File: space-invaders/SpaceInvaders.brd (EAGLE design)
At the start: 101.6 x 95.2 mm, 26 parts, among them J2-J4 TM4C123GXL, J3-J1 TM4C123GXL, J5 Nokia_5110, J6 Nokia_5110, J7 9V, U1 LM7805CT

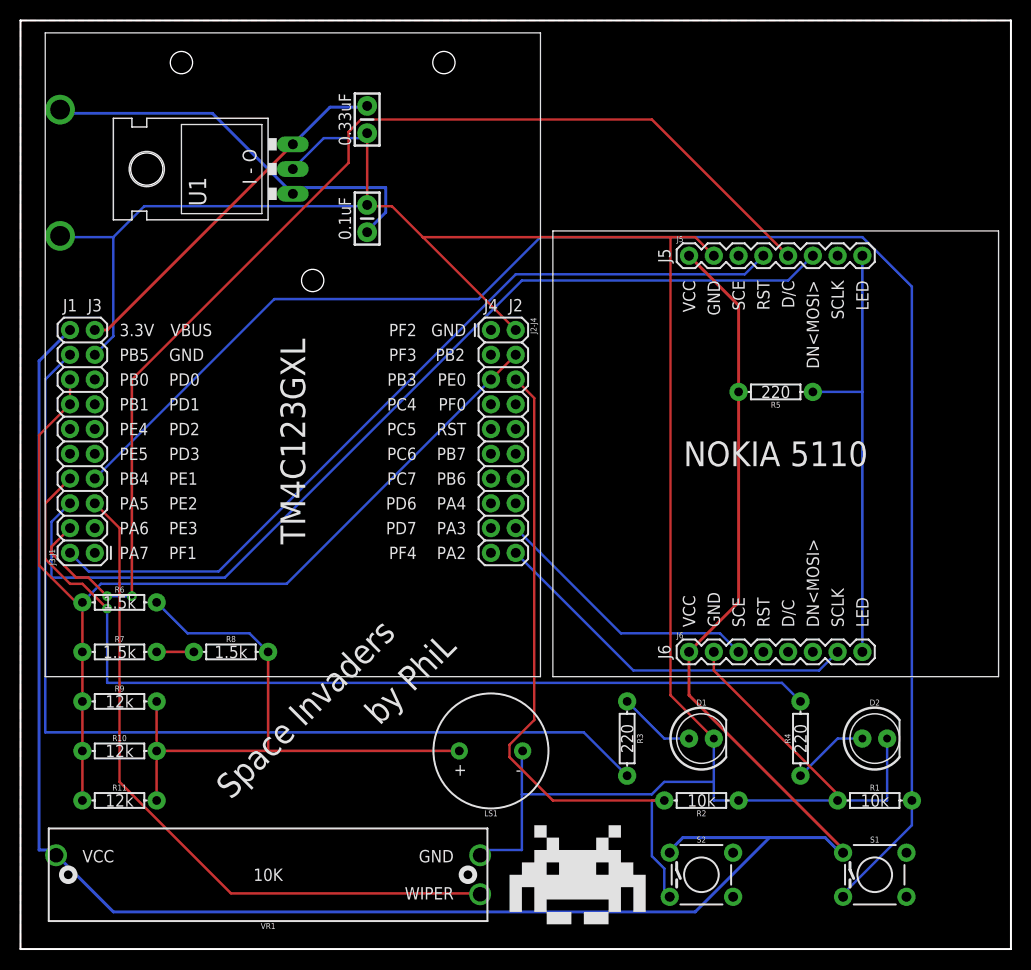
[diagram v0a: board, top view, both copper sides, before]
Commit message: Rip off Autorouter. Will route by hand.
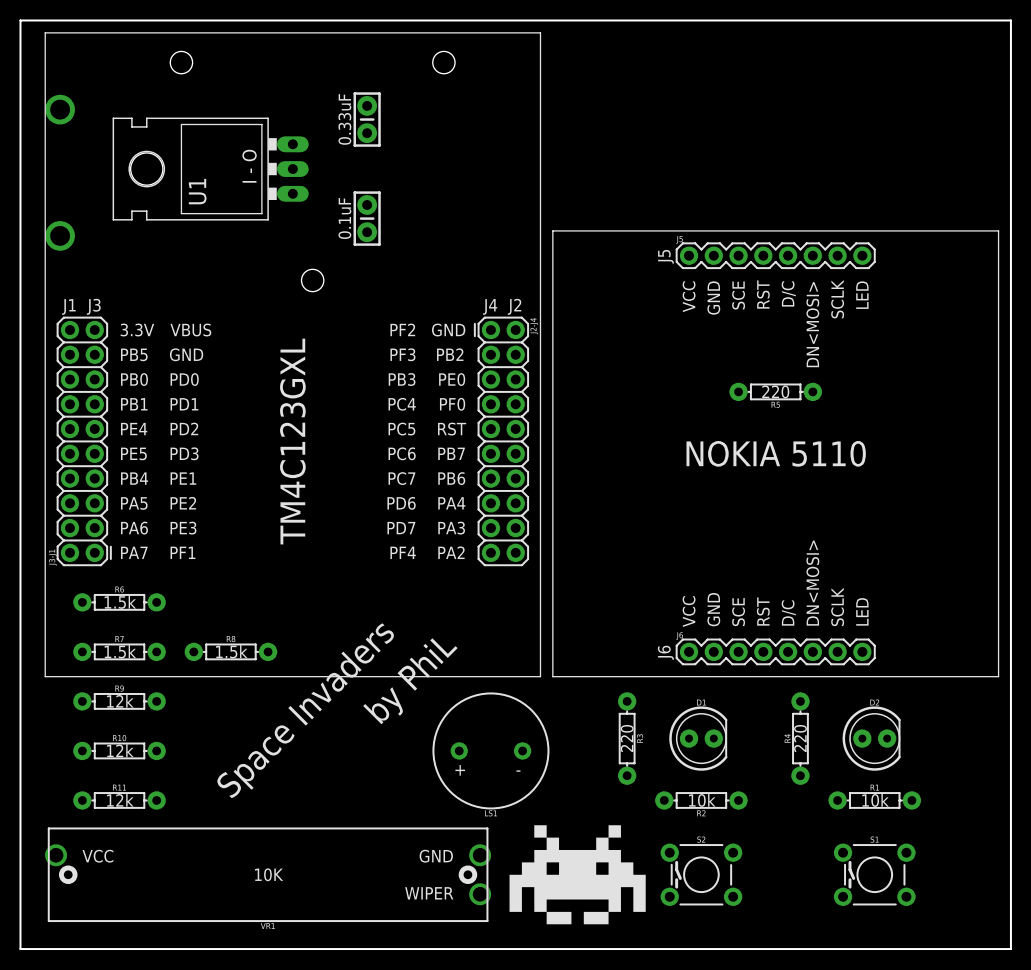
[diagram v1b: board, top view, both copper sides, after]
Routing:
- net GND: track 253.1 -> 0.00 mm
- net 3.3V: track 226.5 -> 0.00 mm
- net PE1: track 161.7 -> 0.00 mm
- net PA6: track 121.7 -> 0.00 mm, vias 2 -> 0
- net PB2: track 101.9 -> 0.00 mm
- net PB5: track 101.3 -> 0.00 mm
- net PA5: track 100.2 -> 0.00 mm
- net PB4: track 97.3 -> 0.00 mm, vias 1 -> 0
- net PA7: track 85.3 -> 0.00 mm
- net PE2: track 71.4 -> 0.00 mm
- net PE0: track 70.3 -> 0.00 mm
- net DAC_OUT: track 64.9 -> 0.00 mm
- net LED: track 45.7 -> 0.00 mm
- net 9V: track 43.0 -> 0.00 mm
- net PA2: track 38.8 -> 0.00 mm
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- removed copper zone on layer 1, net GND

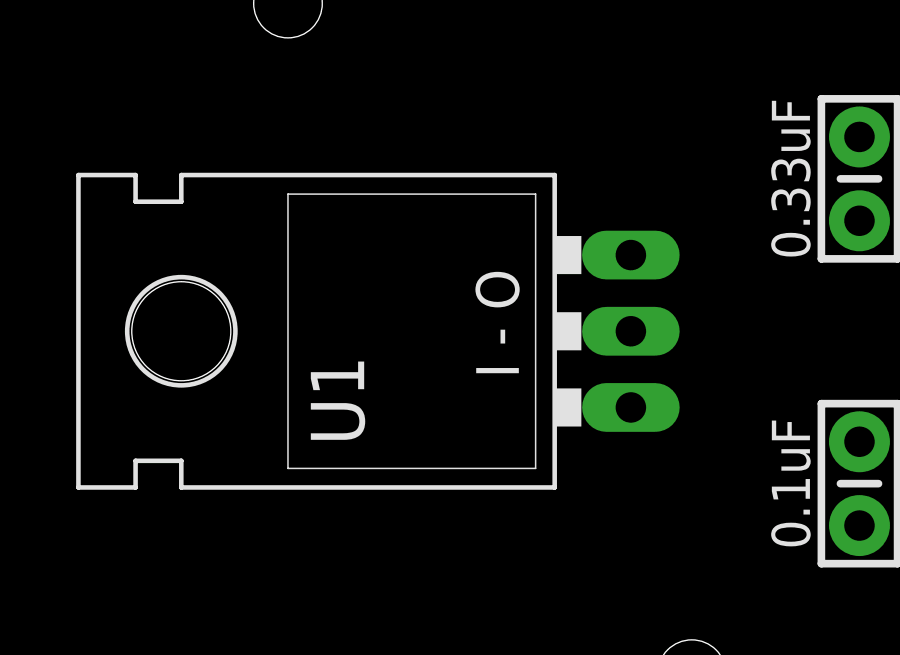
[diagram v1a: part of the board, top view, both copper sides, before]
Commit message: Connect nets & Apply schematic convention
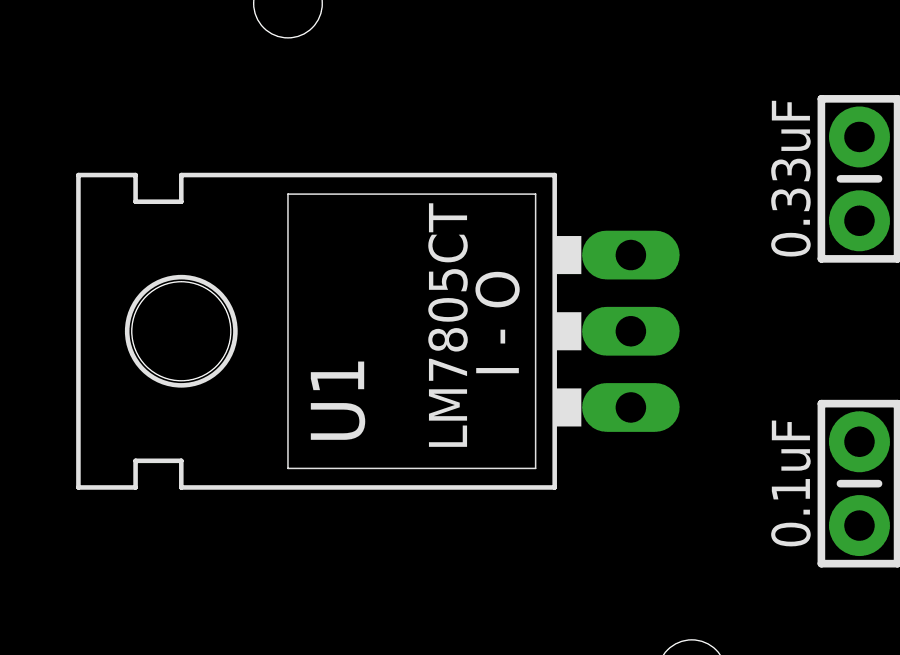
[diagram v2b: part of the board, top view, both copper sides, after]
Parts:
- J5, J6: value Nokia_5110 -> NOKIA_5110
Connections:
- removed net D/C: J6.5
- removed net DN<MOSI>: J6.6
- removed net PE0: J2-J4.6, R2.P$2, S2.3
- removed net RST: J6.4
- removed net SCE: J5.3
- removed net SCLK: J5.7
- new net DAC: J2-J4.4, J2-J4.5, J3-J1.14, J3-J1.16, R10.P$1, R11.P$1, R6.P$1, R7.P$1, R9.P$1
- net PA2: now also J5.7
- net PA3: now also J5.3
- net PA5: now also J6.6
- net PA6: now also J6.5
- net PA7: now also J6.4
- net PB2: now also J2-J4.6, R2.P$2, S2.3; no longer J2-J4.4, J2-J4.5, J3-J1.14, J3-J1.16, R10.P$1, R11.P$1, R6.P$1, R7.P$1, R9.P$1
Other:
- board text added: "LM7805CT"
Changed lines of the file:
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@@
 <?xml version="1.0" encoding="utf-8"?>
 <!DOCTYPE eagle SYSTEM "eagle.dtd">
-<eagle version="8.0.0">
+<eagle version="8.0.1">
 <drawing>
 <settings>
@@
 <text x="77.47" y="57.15" size="1.27" layer="21" font="vector" ratio="10" align="center">220</text>
 <text x="23.495" y="80.264" size="1.4224" layer="21" font="vector" ratio="10" rot="R90" align="center">I - O</text>
+<text x="21.844" y="80.137" size="1.27" layer="21" ratio="10" rot="R90" align="center">LM7805CT</text>
 </plain>
 <attributes>
@@
 <element name="J2-J4" library="SparkFun-Connectors" package="2X10" value="TM4C123GXL" x="48.26" y="63.5" rot="R270"/>
 <element name="J3-J1" library="SparkFun-Connectors" package="2X10" value="TM4C123GXL" x="7.62" y="40.64" rot="R90"/>
-<element name="J5" library="SparkFun-Connectors" package="1X08" value="Nokia_5110" x="68.58" y="71.12">
+<element name="J5" library="SparkFun-Connectors" package="1X08" value="NOKIA_5110" x="68.58" y="71.12">
 <attribute name="PROD_ID" value="CONN-08438" x="68.58" y="71.12" size="1.778" layer="27" display="off"/>
 </element>
-<element name="J6" library="SparkFun-Connectors" package="1X08" value="Nokia_5110" x="68.58" y="30.48">
+<element name="J6" library="SparkFun-Connectors" package="1X08" value="NOKIA_5110" x="68.58" y="30.48">
 <attribute name="PROD_ID" value="CONN-08438" x="68.58" y="30.48" size="1.778" layer="27" display="off"/>
 </element>
@@
 <contactref element="J6" pad="7"/>
 <contactref element="J2-J4" pad="20"/>
+<contactref element="J5" pad="7"/>
+<wire x1="83.82" y1="30.48" x2="83.82" y2="71.12" width="0" layer="19" extent="1-1"/>
 <wire x1="50.8" y1="40.64" x2="83.82" y2="30.48" width="0" layer="19" extent="1-1"/>
 </signal>
@@
 <contactref element="J3-J1" pad="2"/>
 <contactref element="J5" pad="4"/>
-<wire x1="5.08" y1="40.64" x2="76.2" y2="71.12" width="0" layer="19" extent="1-1"/>
+<contactref element="J6" pad="4"/>
+<wire x1="76.2" y1="30.48" x2="76.2" y2="71.12" width="0" layer="19" extent="1-1"/>
+<wire x1="5.08" y1="40.64" x2="76.2" y2="30.48" width="0" layer="19" extent="1-1"/>
 </signal>
 <signal name="PA6">
 <contactref element="J3-J1" pad="4"/>
 <contactref element="J5" pad="5"/>
-<wire x1="5.08" y1="43.18" x2="78.74" y2="71.12" width="0" layer="19" extent="1-1"/>
+<contactref element="J6" pad="5"/>
+<wire x1="78.74" y1="30.48" x2="78.74" y2="71.12" width="0" layer="19" extent="1-1"/>
+<wire x1="5.08" y1="43.18" x2="78.74" y2="30.48" width="0" layer="19" extent="1-1"/>
 </signal>
 <signal name="PA5">
 <contactref element="J3-J1" pad="6"/>
 <contactref element="J5" pad="6"/>
-<wire x1="5.08" y1="45.72" x2="81.28" y2="71.12" width="0" layer="19" extent="1-1"/>
+<contactref element="J6" pad="6"/>
+<wire x1="81.28" y1="30.48" x2="81.28" y2="71.12" width="0" layer="19" extent="1-1"/>
+<wire x1="5.08" y1="45.72" x2="81.28" y2="30.48" width="0" layer="19" extent="1-1"/>
 </signal>
 <signal name="PB4">
@@
 <wire x1="5.08" y1="48.26" x2="80.01" y2="25.4" width="0" layer="19" extent="1-1"/>
 </signal>
-<signal name="PB2">
+<signal name="DAC">
 <contactref element="R6" pad="P$1"/>
 <contactref element="R7" pad="P$1"/>
@@
 <contactref element="J6" pad="3"/>
 <contactref element="J2-J4" pad="18"/>
-<wire x1="50.8" y1="43.18" x2="73.66" y2="30.48" width="0" layer="19" extent="1-1"/>
+<contactref element="J5" pad="3"/>
+<wire x1="50.8" y1="43.18" x2="73.66" y2="71.12" width="0" layer="19" extent="1-1"/>
+<wire x1="73.66" y1="30.48" x2="50.8" y2="43.18" width="0" layer="19" extent="1-1"/>
 </signal>
 <signal name="3.3V" class="1">
@@
 <contactref element="J3-J1" pad="15"/>
 </signal>
-<signal name="RST">
-<contactref element="J6" pad="4"/>
-</signal>
-<signal name="D/C">
-<contactref element="J6" pad="5"/>
-</signal>
-<signal name="DN&lt;MOSI&gt;">
-<contactref element="J6" pad="6"/>
-</signal>
-<signal name="SCE">
-<contactref element="J5" pad="3"/>
-</signal>
-<signal name="SCLK">
-<contactref element="J5" pad="7"/>
-</signal>
 <signal name="PF2">
 <contactref element="J2-J4" pad="1"/>
@@
 <wire x1="7.62" y1="48.26" x2="84.3788" y2="5.3594" width="0" layer="19" extent="1-1"/>
 </signal>
-<signal name="PE0">
+<signal name="PB2">
 <contactref element="R2" pad="P$2"/>
 <contactref element="J2-J4" pad="6"/>

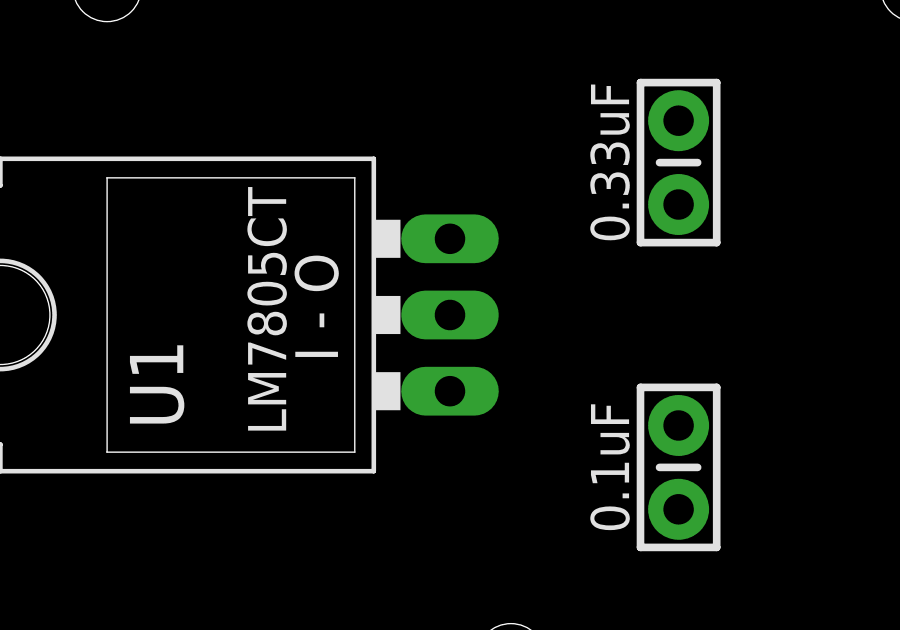
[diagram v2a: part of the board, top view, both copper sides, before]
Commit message: Expand & make more space in schematic
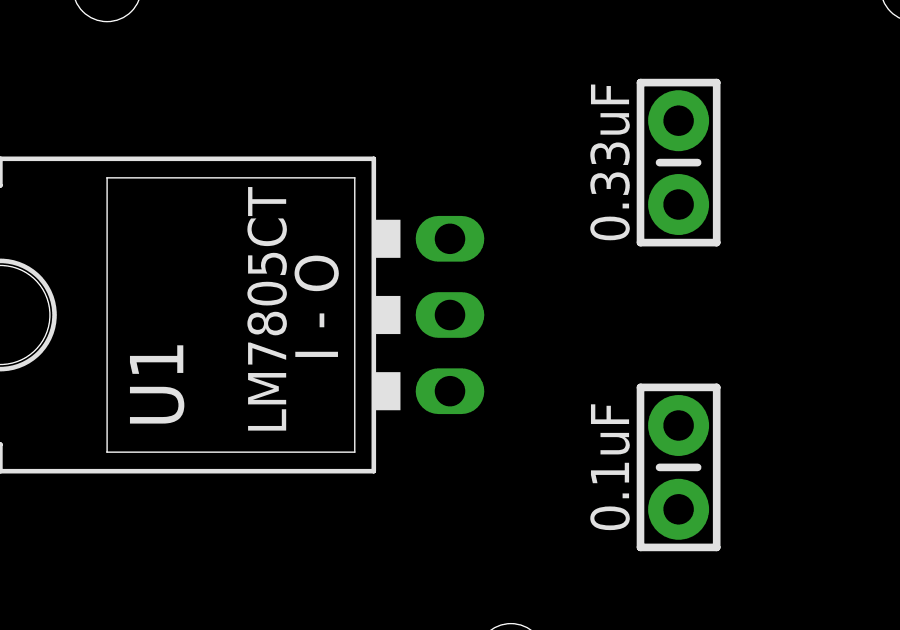
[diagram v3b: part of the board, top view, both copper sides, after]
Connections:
- net PB2 renamed PE0
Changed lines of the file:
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@@
 </class>
 </classes>
-<designrules name="SparkFun">
-<description language="en">&lt;b&gt;SparkFun EAGLE Design Rules&lt;/b&gt;
-&lt;p&gt;
-The default Design Rules have been set to cover
-a wide range of applications. Your particular design
-may have different requirements, so please make the
-necessary adjustments and save your customized
-design rules under a new name.</description>
+<designrules name="OthermillDRC_1_32_v2">
+<description language="en">&lt;b&gt;Othermill EAGLE Design Rules v2&lt;/b&gt;&lt;p&gt;DRC for Othermill, 1/32&quot; tool&lt;/p&gt;&lt;b&gt;-- Rules --&lt;/b&gt;&lt;li&gt;8 mil traces&lt;/li&gt;&lt;li&gt;31.26mil clearance&lt;/li&gt;</description>
 <param name="layerSetup" value="(1*16)"/>
 <param name="mtCopper" value="0.035mm 0.035mm 0.035mm 0.035mm 0.035mm 0.035mm 0.035mm 0.035mm 0.035mm 0.035mm 0.035mm 0.035mm 0.035mm 0.035mm 0.035mm 0.035mm"/>
 <param name="mtIsolate" value="1.5mm 0.15mm 0.2mm 0.15mm 0.2mm 0.15mm 0.2mm 0.15mm 0.2mm 0.15mm 0.2mm 0.15mm 0.2mm 0.15mm 0.2mm"/>
-<param name="mdWireWire" value="8mil"/>
-<param name="mdWirePad" value="8mil"/>
-<param name="mdWireVia" value="8mil"/>
-<param name="mdPadPad" value="8mil"/>
-<param name="mdPadVia" value="8mil"/>
-<param name="mdViaVia" value="8mil"/>
-<param name="mdSmdPad" value="8mil"/>
-<param name="mdSmdVia" value="8mil"/>
-<param name="mdSmdSmd" value="8mil"/>
+<param name="mdWireWire" value="0.794003125mm"/>
+<param name="mdWirePad" value="0.794003125mm"/>
+<param name="mdWireVia" value="0.794003125mm"/>
+<param name="mdPadPad" value="0.794003125mm"/>
+<param name="mdPadVia" value="0.794003125mm"/>
+<param name="mdViaVia" value="0.794003125mm"/>
+<param name="mdSmdPad" value="0mil"/>
+<param name="mdSmdVia" value="0mil"/>
+<param name="mdSmdSmd" value="0mil"/>
 <param name="mdViaViaSameLayer" value="8mil"/>
 <param name="mnLayersViaInSmd" value="2"/>
-<param name="mdCopperDimension" value="10mil"/>
-<param name="mdDrill" value="8mil"/>
+<param name="mdCopperDimension" value="0mil"/>
+<param name="mdDrill" value="1mil"/>
 <param name="mdSmdStop" value="0mil"/>
 <param name="msWidth" value="8mil"/>
-<param name="msDrill" value="20mil"/>
+<param name="msDrill" value="0.8mm"/>
 <param name="msMicroVia" value="9.99mm"/>
 <param name="msBlindViaRatio" value="0.5"/>
@@
 <param name="rvMicroViaOuter" value="0.25"/>
 <param name="rvMicroViaInner" value="0.25"/>
-<param name="rlMinPadTop" value="12mil"/>
+<param name="rlMinPadTop" value="10mil"/>
 <param name="rlMaxPadTop" value="20mil"/>
 <param name="rlMinPadInner" value="10mil"/>
 <param name="rlMaxPadInner" value="20mil"/>
-<param name="rlMinPadBottom" value="12mil"/>
+<param name="rlMinPadBottom" value="10mil"/>
 <param name="rlMaxPadBottom" value="20mil"/>
 <param name="rlMinViaOuter" value="10mil"/>
 <param name="rlMaxViaOuter" value="20mil"/>
-<param name="rlMinViaInner" value="10mil"/>
+<param name="rlMinViaInner" value="8mil"/>
 <param name="rlMaxViaInner" value="20mil"/>
 <param name="rlMinMicroViaOuter" value="4mil"/>
@@
 <param name="psBottom" value="-1"/>
 <param name="psFirst" value="-1"/>
-<param name="psElongationLong" value="100"/>
+<param name="psElongationLong" value="50"/>
 <param name="psElongationOffset" value="100"/>
-<param name="mvStopFrame" value="1"/>
-<param name="mvCreamFrame" value="0"/>
-<param name="mlMinStopFrame" value="4mil"/>
-<param name="mlMaxStopFrame" value="4mil"/>
-<param name="mlMinCreamFrame" value="0mil"/>
-<param name="mlMaxCreamFrame" value="0mil"/>
-<param name="mlViaStopLimit" value="25mil"/>
-<param name="srRoundness" value="0"/>
-<param name="srMinRoundness" value="0mil"/>
-<param name="srMaxRoundness" value="0mil"/>
+<param name="mvStopFrame" value="0.05"/>
+<param name="mvCreamFrame" value="0.05"/>
+<param name="mlMinStopFrame" value="1mil"/>
+<param name="mlMaxStopFrame" value="2mil"/>
+<param name="mlMinCreamFrame" value="2mil"/>
+<param name="mlMaxCreamFrame" value="10mil"/>
+<param name="mlViaStopLimit" value="30mil"/>
+<param name="srRoundness" value="0.1"/>
+<param name="srMinRoundness" value="2mil"/>
+<param name="srMaxRoundness" value="10mil"/>
 <param name="slThermalIsolate" value="10mil"/>
 <param name="slThermalsForVias" value="0"/>
@@
 </signal>
 <signal name="DAC_OUT">
-<contactref element="R6" pad="P$2"/>
-<contactref element="R8" pad="P$2"/>
 <contactref element="R9" pad="P$2"/>
 <contactref element="R10" pad="P$2"/>
 <contactref element="R11" pad="P$2"/>
+<contactref element="R6" pad="P$2"/>
+<contactref element="R8" pad="P$2"/>
 <contactref element="LS1" pad="+"/>
 <wire x1="25.4" y1="30.48" x2="45.01" y2="20.32" width="0" layer="19" extent="1-1"/>
@@
 <signal name="DAC">
 <contactref element="R6" pad="P$1"/>
-<contactref element="R7" pad="P$1"/>
-<contactref element="R9" pad="P$1"/>
-<contactref element="R10" pad="P$1"/>
-<contactref element="R11" pad="P$1"/>
 <contactref element="J2-J4" pad="5"/>
 <contactref element="J2-J4" pad="4"/>
 <contactref element="J3-J1" pad="14"/>
 <contactref element="J3-J1" pad="16"/>
+<contactref element="R7" pad="P$1"/>
+<contactref element="R9" pad="P$1"/>
+<contactref element="R11" pad="P$1"/>
+<contactref element="R10" pad="P$1"/>
 <wire x1="48.26" y1="58.42" x2="50.8" y2="60.96" width="0" layer="19" extent="1-1"/>
 <wire x1="5.08" y1="58.42" x2="48.26" y2="58.42" width="0" layer="19" extent="1-1"/>
@@
 <wire x1="7.62" y1="48.26" x2="84.3788" y2="5.3594" width="0" layer="19" extent="1-1"/>
 </signal>
-<signal name="PB2">
+<signal name="PE0">
 <contactref element="R2" pad="P$2"/>
 <contactref element="J2-J4" pad="6"/>
@@
 </signal>
 </signals>
+<errors>
+</errors>
 </board>
 </drawing>
